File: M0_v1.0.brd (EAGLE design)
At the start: 68.6 x 53.3 mm, 61 parts, among them CN1 POWER_JACK, CN2 47346-0001, CN3 DIGITAL10, CN4 DIGITAL8, CN5 ICSP, CN6 POWER8, CN7 ANALOG6, CN8 SWD, CN9 UART, IC1 AMS1117-5.0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

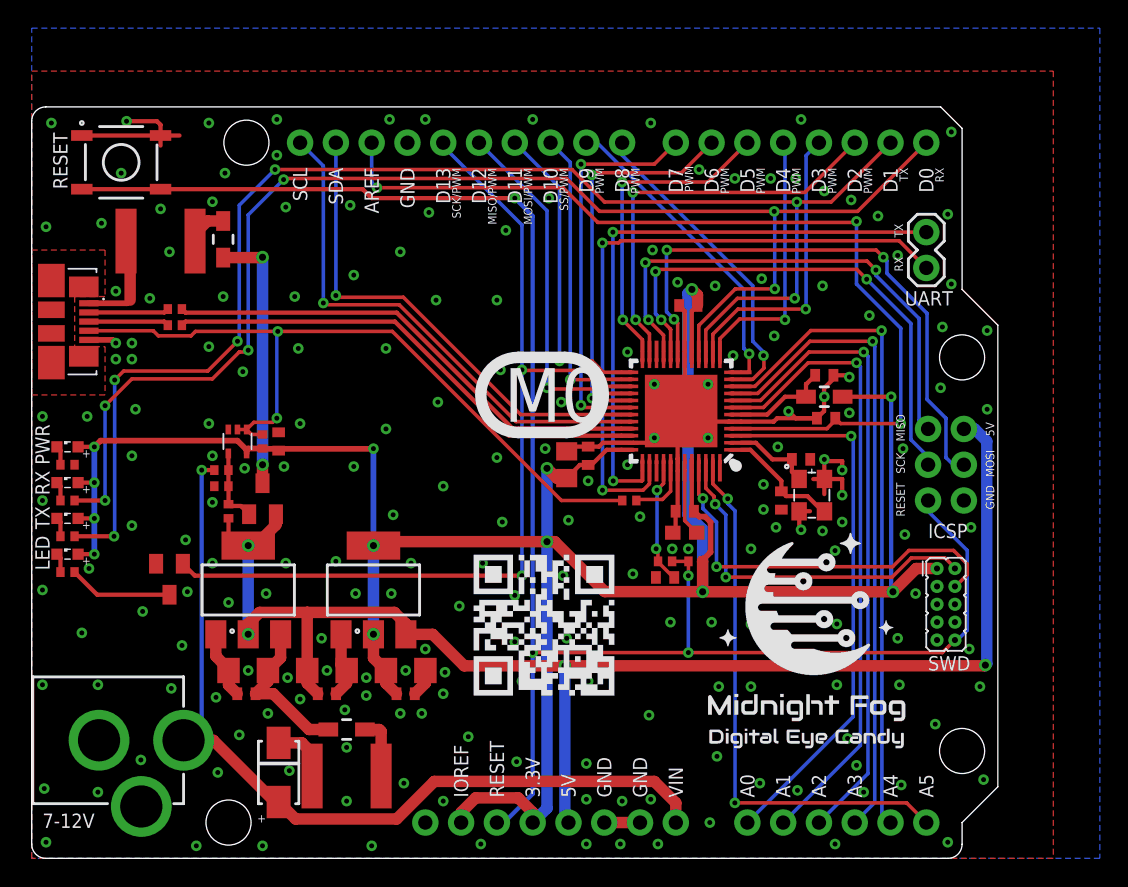
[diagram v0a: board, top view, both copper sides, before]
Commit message: Fixed TX_LED and RT_LED signals
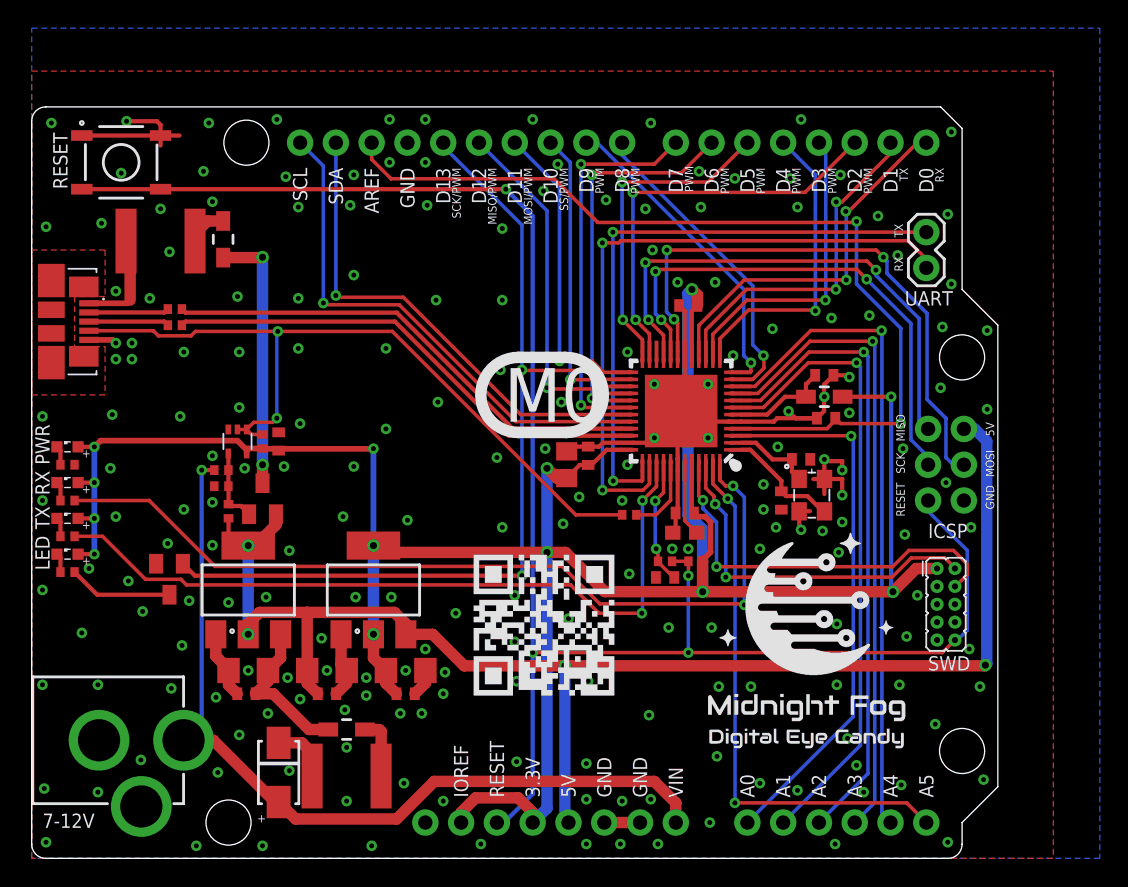
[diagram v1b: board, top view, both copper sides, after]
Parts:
- moved R6 1.02 mm to (42.4, 24.4)
- moved C16 0.13 mm to (46.4, 24.5)
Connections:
- new net N$6: U2.48
- new net RX_LED: R8.1, U1.48, U2.48
- new net TX_LED: R9.1, U1.39, U2.39
- net D0_RX: no longer R8.1
- net D1_TX: no longer R9.1
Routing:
- net D1_TX: track 100.0 -> 25.0 mm, vias 6 -> 2
- net D0_RX: track 97.1 -> 27.1 mm, vias 6 -> 2
- net RX_LED: track 0.00 -> 62.0 mm, vias 0 -> 2
- net TX_LED: track 0.00 -> 53.9 mm, vias 0 -> 2
- net D4: track 19.6 -> 22.3 mm
- net AREF: track 66.8 -> 65.9 mm, vias 3 -> 2
- net D3_PWM: track 21.6 -> 22.4 mm
- net USB_EN: track 5.00 -> 5.79 mm
- net GND: vias 206 -> 208

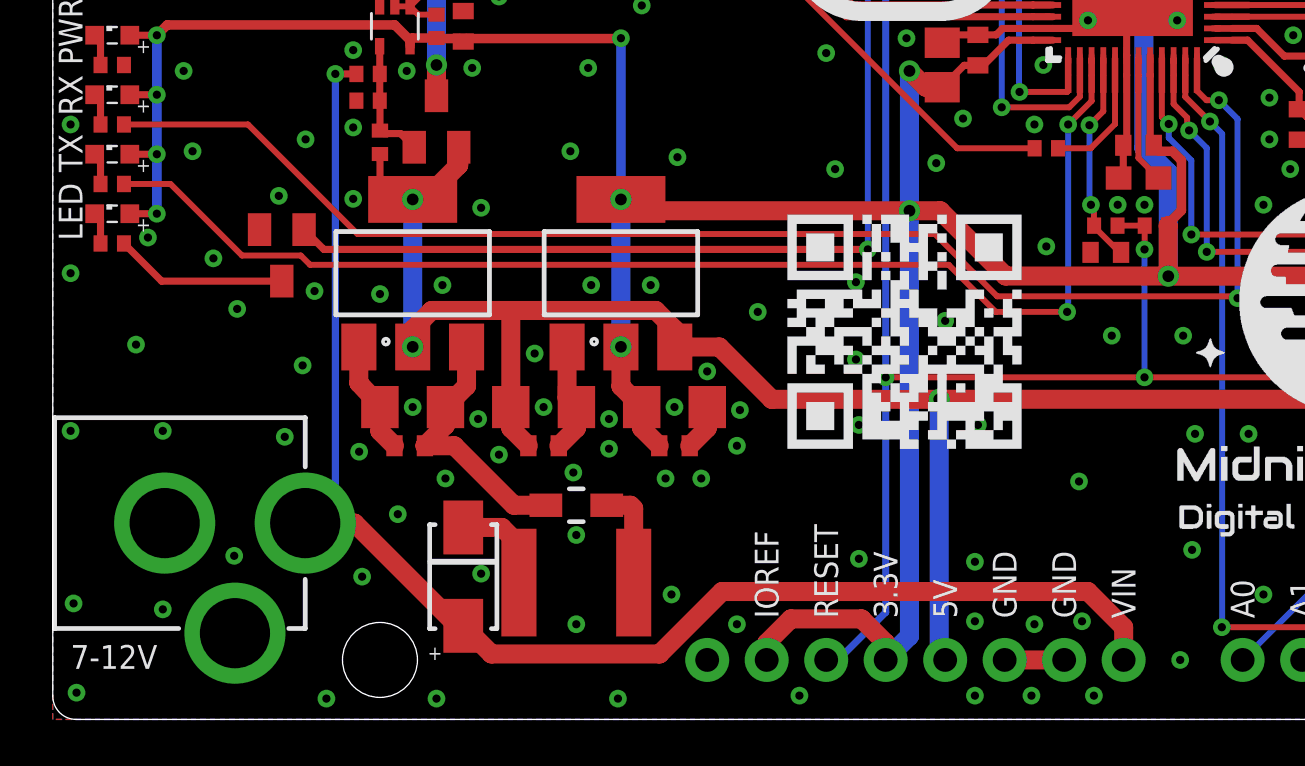
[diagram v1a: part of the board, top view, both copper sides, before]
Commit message: Fix some eagle bug. Add more connections around power jack ground.
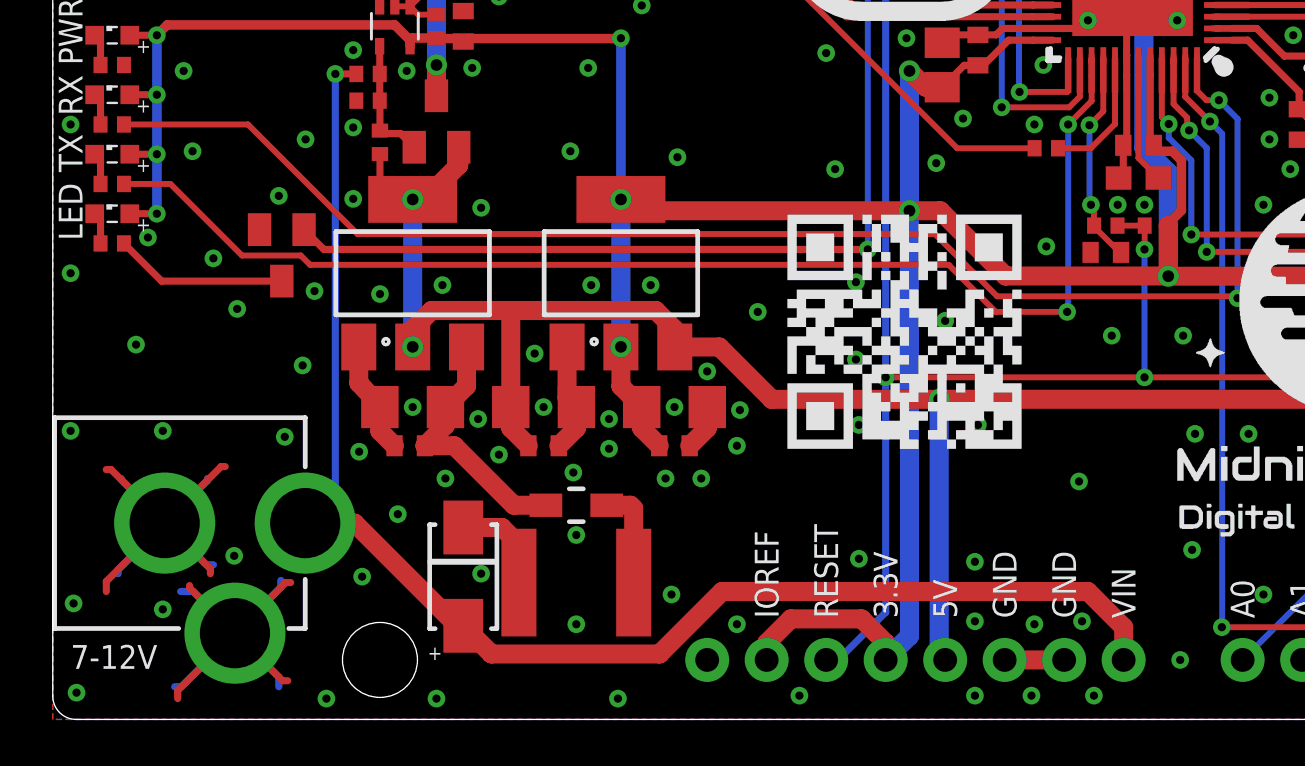
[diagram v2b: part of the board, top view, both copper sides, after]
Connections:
- removed net N$6: U2.48
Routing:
- net GND: track 70.6 -> 121.4 mm
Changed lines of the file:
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@@
 <via x="27.94" y="49.403" extent="1-16" drill="0.35"/>
 <via x="64.897" y="26.67" extent="1-16" drill="0.35"/>
+<wire x1="7.779" y1="3.682" x2="5.842" y2="5.619" width="0.3048" layer="1"/>
+<wire x1="5.842" y1="5.619" x2="5.842" y2="5.715" width="0.3048" layer="1"/>
+<wire x1="7.779" y1="3.682" x2="9.81" y2="1.651" width="0.3048" layer="1"/>
+<wire x1="9.81" y1="1.651" x2="10.033" y2="1.651" width="0.3048" layer="1"/>
+<wire x1="7.779" y1="3.682" x2="9.939" y2="5.842" width="0.3048" layer="1"/>
+<wire x1="9.939" y1="5.842" x2="10.16" y2="5.842" width="0.3048" layer="1"/>
+<wire x1="7.779" y1="3.682" x2="5.334" y2="1.237" width="0.3048" layer="1"/>
+<wire x1="5.334" y1="1.237" x2="5.334" y2="0.889" width="0.3048" layer="1"/>
+<wire x1="4.779" y1="8.382" x2="2.493" y2="10.668" width="0.3048" layer="1"/>
+<wire x1="2.493" y1="10.668" x2="2.286" y2="10.668" width="0.3048" layer="1"/>
+<wire x1="4.779" y1="8.382" x2="7.192" y2="10.795" width="0.3048" layer="1"/>
+<wire x1="7.192" y1="10.795" x2="7.366" y2="10.795" width="0.3048" layer="1"/>
+<wire x1="4.779" y1="8.382" x2="2.286" y2="5.889" width="0.3048" layer="1"/>
+<wire x1="2.286" y1="5.889" x2="2.286" y2="5.461" width="0.3048" layer="1"/>
+<wire x1="4.779" y1="8.382" x2="6.731" y2="6.43" width="0.3048" layer="1"/>
+<wire x1="6.731" y1="6.43" x2="6.731" y2="6.223" width="0.3048" layer="1"/>
+<wire x1="4.779" y1="8.382" x2="6.604" y2="10.207" width="0.3048" layer="16"/>
+<wire x1="6.604" y1="10.207" x2="6.604" y2="10.287" width="0.3048" layer="16"/>
+<wire x1="4.779" y1="8.382" x2="2.921" y2="10.24" width="0.3048" layer="16"/>
+<wire x1="2.921" y1="10.24" x2="2.921" y2="10.287" width="0.3048" layer="16"/>
+<wire x1="4.779" y1="8.382" x2="2.794" y2="6.397" width="0.3048" layer="16"/>
+<wire x1="2.794" y1="6.397" x2="2.794" y2="6.223" width="0.3048" layer="16"/>
+<wire x1="4.779" y1="8.382" x2="6.557" y2="6.604" width="0.3048" layer="16"/>
+<wire x1="6.557" y1="6.604" x2="6.858" y2="6.604" width="0.3048" layer="16"/>
+<wire x1="7.779" y1="3.682" x2="6" y2="5.461" width="0.3048" layer="16"/>
+<wire x1="6" y1="5.461" x2="5.461" y2="5.461" width="0.3048" layer="16"/>
+<wire x1="7.779" y1="3.682" x2="9.743328125" y2="5.646328125" width="0.3048" layer="16"/>
+<wire x1="9.743328125" y1="5.646328125" x2="9.743328125" y2="5.933328125" width="0.3048" layer="16"/>
+<wire x1="7.779" y1="3.682" x2="5.494" y2="1.397" width="0.3048" layer="16"/>
+<wire x1="5.494" y1="1.397" x2="5.207" y2="1.397" width="0.3048" layer="16"/>
+<wire x1="7.779" y1="3.682" x2="9.652" y2="1.809" width="0.3048" layer="16"/>
+<wire x1="9.652" y1="1.809" x2="9.652" y2="1.397" width="0.3048" layer="16"/>
 </signal>
 <signal name="VIN" class="3">
@@
 <wire x1="47.617" y1="21.15595" x2="47.617" y2="21.082" width="0.4064" layer="1"/>
 <wire x1="48.1868" y1="23.86725" x2="47.79705" y2="24.257" width="0.4064" layer="1"/>
-<wire x1="47.005" y1="24.511" x2="47.259" y2="24.257" width="0.4064" layer="1"/>
 <wire x1="47.79705" y1="24.257" x2="47.259" y2="24.257" width="0.4064" layer="1"/>
+<wire x1="47.259" y1="24.257" x2="47.005" y2="24.511" width="0.4064" layer="1"/>
 <wire x1="48.1868" y1="21.72575" x2="47.617" y2="21.15595" width="0.4064" layer="1"/>
 <contactref element="L3" pad="2"/>
@@
 <wire x1="40.513" y1="43.688" x2="40.513" y2="26.1321875" width="0.254" layer="16"/>
 </signal>
-<signal name="N$6">
-<contactref element="U2" pad="48"/>
-</signal>
 <signal name="RX_LED">

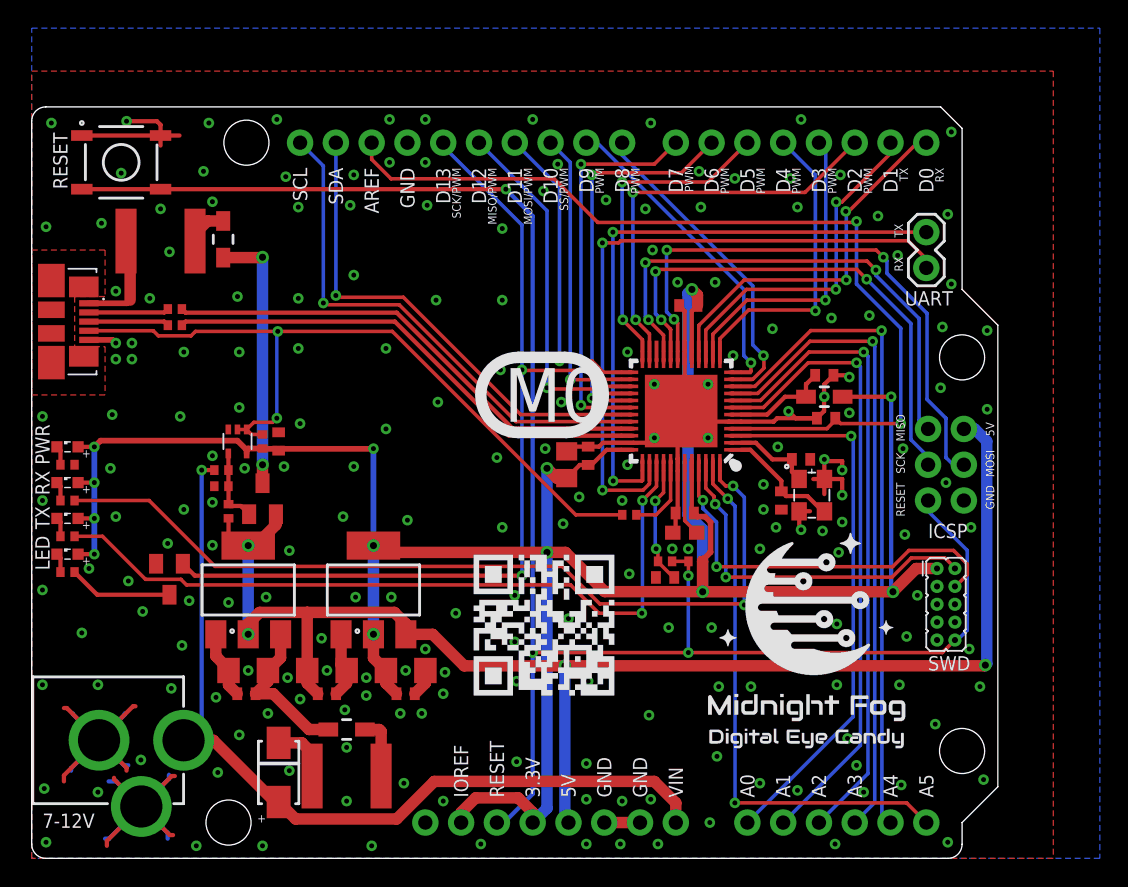
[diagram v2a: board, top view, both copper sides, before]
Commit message: Moved MCU to the right a little with all belongings.
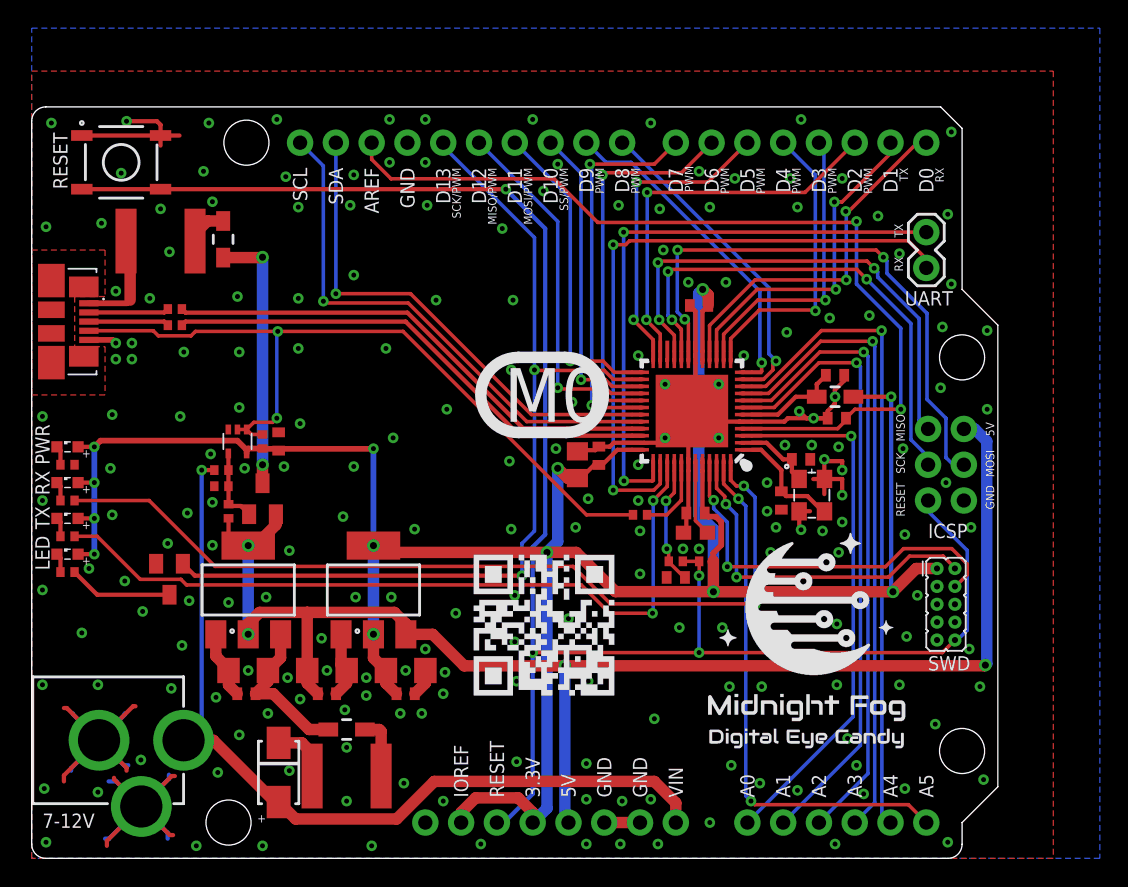
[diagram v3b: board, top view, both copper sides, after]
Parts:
- moved C14 0.76 mm to (40.3, 28.6)
- moved C15 0.76 mm to (47.4, 39.2)
- moved C16 0.76 mm to (47.1, 24.5)
- moved C17 0.76 mm to (38.7, 27.9)
- moved C19 0.76 mm to (57.1, 31.2)
- moved C7 0.76 mm to (47.1, 23.1)
- moved C8 0.76 mm to (45.7, 19.9)
- moved C9 0.76 mm to (57.0, 34.3)
- moved L3 0.76 mm to (57.0, 32.8)
- moved R12 0.76 mm to (47.9, 21.1)
- moved R3 0.76 mm to (45.7, 21.1)
- moved R6 0.76 mm to (43.2, 24.4)
- moved U1 0.76 mm to (46.9, 31.8)
- moved U2 0.76 mm to (46.9, 31.8)
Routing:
- net AREF: track 65.9 -> 64.2 mm
- net GND: track 121.4 -> 120.2 mm, vias 208 -> 210
- net D2: track 29.8 -> 28.7 mm
- net A5: track 39.2 -> 38.2 mm
- net D5_PWM: track 23.5 -> 22.5 mm
- net SPI_SCK: track 37.3 -> 36.3 mm
- net SPI_MISO: track 37.2 -> 36.2 mm
- net D9_PWM: track 23.1 -> 24.0 mm
- net UART_RX: track 47.1 -> 46.2 mm
- net D3_PWM: track 22.4 -> 21.6 mm
- net UART_TX: track 43.5 -> 42.8 mm
- net A3: track 46.5 -> 45.8 mm
- net A1: track 45.4 -> 44.6 mm
- net SPI_MOSI: track 41.5 -> 40.7 mm
- net XUSB_EN: track 54.1 -> 54.9 mm
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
